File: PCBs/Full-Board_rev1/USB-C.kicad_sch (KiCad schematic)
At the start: 5 parts, among them J1 TYPE-C-31-M-12

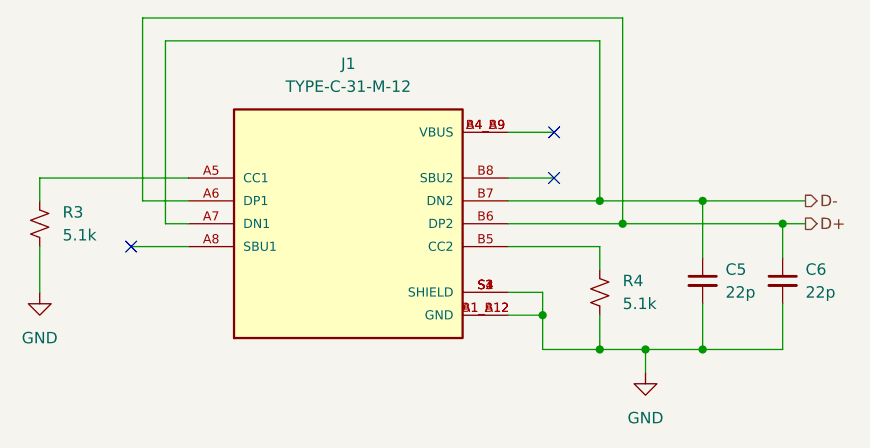
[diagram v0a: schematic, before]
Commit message: added ESP32 peripherals
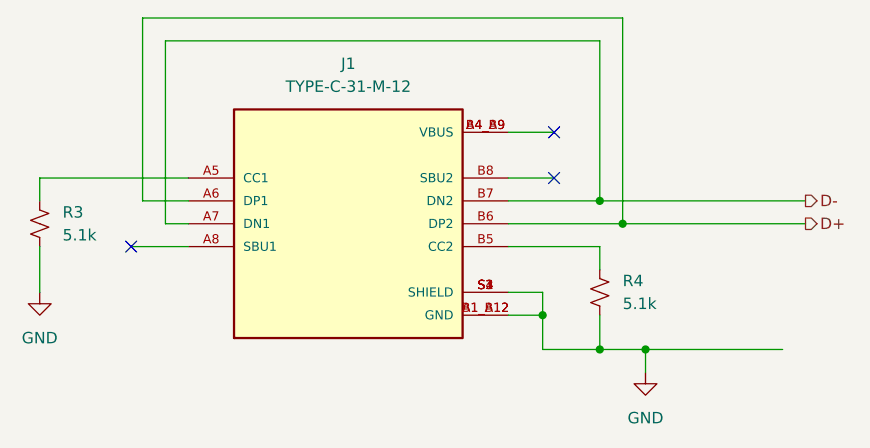
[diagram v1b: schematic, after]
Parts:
- removed C5, C6: 22p, symbol Device:C_Small
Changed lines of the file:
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@@
-	)
-	(junction
-		(at 180.34 115.57)
-		(diameter 0)
-		(color 0 0 0 0)
-	)
-	(junction
-		(at 189.23 101.6)
-		(diameter 0)
-		(color 0 0 0 0)
 	)
 	(junction
@@
 	)
 	(junction
-		(at 180.34 99.06)
-		(diameter 0)
-		(color 0 0 0 0)
-	)
-	(junction
 		(at 168.91 115.57)
 		(diameter 0)
@@
 	(wire
 		(pts
-			(xy 171.45 101.6) (xy 189.23 101.6)
+			(xy 171.45 101.6) (xy 191.77 101.6)
 		)
 		(stroke
@@
 	(wire
 		(pts
-			(xy 180.34 115.57) (xy 189.23 115.57)
-		)
-		(stroke
-			(width 0)
-			(type default)
-		)
-	)
-	(wire
-		(pts
 			(xy 158.75 96.52) (xy 163.83 96.52)
 		)
@@
 	(wire
 		(pts
-			(xy 180.34 99.06) (xy 191.77 99.06)
-		)
-		(stroke
-			(width 0)
-			(type default)
-		)
-	)
-	(wire
-		(pts
 			(xy 158.75 101.6) (xy 171.45 101.6)
 		)
@@
 	(wire
 		(pts
-			(xy 168.91 99.06) (xy 180.34 99.06)
+			(xy 168.91 99.06) (xy 191.77 99.06)
 		)
 		(stroke
@@
 	(wire
 		(pts
-			(xy 189.23 115.57) (xy 189.23 110.49)
-		)
-		(stroke
-			(width 0)
-			(type default)
-		)
-	)
-	(wire
-		(pts
 			(xy 158.75 99.06) (xy 168.91 99.06)
 		)
@@
 	(wire
 		(pts
-			(xy 173.99 115.57) (xy 180.34 115.57)
+			(xy 173.99 115.57) (xy 189.23 115.57)
 		)
 		(stroke
@@
 	(wire
 		(pts
-			(xy 189.23 101.6) (xy 189.23 105.41)
-		)
-		(stroke
-			(width 0)
-			(type default)
-		)
-	)
-	(wire
-		(pts
 			(xy 116.84 104.14) (xy 123.19 104.14)
 		)
@@
 	(wire
 		(pts
-			(xy 189.23 101.6) (xy 191.77 101.6)
-		)
-		(stroke
-			(width 0)
-			(type default)
-		)
-	)
-	(wire
-		(pts
 			(xy 120.65 81.28) (xy 168.91 81.28)
 		)
@@
 		(pts
 			(xy 168.91 115.57) (xy 173.99 115.57)
-		)
-		(stroke
-			(width 0)
-			(type default)
-		)
-	)
-	(wire
-		(pts
-			(xy 180.34 110.49) (xy 180.34 115.57)
-		)
-		(stroke
-			(width 0)
-			(type default)
-		)
-	)
-	(wire
-		(pts
-			(xy 180.34 99.06) (xy 180.34 105.41)
 		)
 		(stroke
@@
 			)
 			(justify left)
-		)
-	)
-	(symbol
-		(lib_id "Device:C_Small")
-		(at 180.34 107.95 0)
-		(unit 1)
-		(exclude_from_sim no)
-		(in_bom yes)
-		(on_board yes)
-		(dnp no)
-		(fields_autoplaced yes)
-		(property "Reference" "C5"
-			(at 182.88 106.6862 0)
-			(effects
-				(font
-					(size 1.27 1.27)
-				)
-				(justify left)
-			)
-		)
-		(property "Value" "22p"
-			(at 182.88 109.2262 0)
-			(effects
-				(font
-					(size 1.27 1.27)
-				)
-				(justify left)
-			)
-		)
-		(property "Footprint" ""
-			(at 180.34 107.95 0)
-			(effects
-				(font
-					(size 1.27 1.27)
-				)
-				(hide yes)
-			)
-		)
-		(property "Datasheet" "~"
-			(at 180.34 107.95 0)
-			(effects
-				(font
-					(size 1.27 1.27)
-				)
-				(hide yes)
-			)
-		)
-		(property "Description" "Unpolarized capacitor, small symbol"
-			(at 180.34 107.95 0)
-			(effects
-				(font
-					(size 1.27 1.27)
-				)
-				(hide yes)
-			)
-		)
-		(pin "2"
-		)
-		(pin "1"
-		)
-		(instances
-			(project ""
-				(path "/2dd686ed-aa28-474a-bf3c-628eebb4b373/4c56a540-4f9c-4723-9763-cba6b0ba4e1b"
-					(reference "C5")
-					(unit 1)
-				)
-			)
 		)
 	)
@@
 					(unit 1)
 				)
-			)
-		)
-	)
-	(symbol
-		(lib_id "Device:C_Small")
-		(at 189.23 107.95 0)
-		(unit 1)
-		(exclude_from_sim no)
-		(in_bom yes)
-		(on_board yes)
-		(dnp no)
-		(fields_autoplaced yes)
-		(property "Reference" "C6"
-			(at 191.77 106.6862 0)
-			(effects
-				(font
-					(size 1.27 1.27)
-				)
-				(justify left)
-			)
-		)
-		(property "Value" "22p"
-			(at 191.77 109.2262 0)
-			(effects
-				(font
-					(size 1.27 1.27)
-				)
-				(justify left)
-			)
-		)
-		(property "Footprint" ""
-			(at 189.23 107.95 0)
-			(effects
-				(font
-					(size 1.27 1.27)
-				)
-				(hide yes)
-			)
-		)
-		(property "Datasheet" "~"
-			(at 189.23 107.95 0)
-			(effects
-				(font
-					(size 1.27 1.27)
-				)
-				(hide yes)
-			)
-		)
-		(property "Description" "Unpolarized capacitor, small symbol"
-			(at 189.23 107.95 0)
-			(effects
-				(font
-					(size 1.27 1.27)
-				)
-				(hide yes)
-			)
-		)
-		(pin "1"
-		)
-		(pin "2"
-		)
-		(instances
-			(project ""
-				(path "/2dd686ed-aa28-474a-bf3c-628eebb4b373/4c56a540-4f9c-4723-9763-cba6b0ba4e1b"
-					(reference "C6")
-					(unit 1)
-				)

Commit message: Added footprints for main board components
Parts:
- R3, R4: footprint (none) -> Connector_PinHeader_2.54mm:PinHeader_1x02_P2.54mm_Vertical
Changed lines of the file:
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@@
 			)
 		)
-		(property "Footprint" ""
+		(property "Footprint" "Connector_PinHeader_2.54mm:PinHeader_1x02_P2.54mm_Vertical"
 			(at 106.68 101.6 0)
 			(effects
@@
 			)
 		)
-		(property "Footprint" ""
+		(property "Footprint" "Connector_PinHeader_2.54mm:PinHeader_1x02_P2.54mm_Vertical"
 			(at 168.91 109.22 0)
 			(effects

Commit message: Redid some faulty footprint assignments
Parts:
- R3, R4: footprint Connector_PinHeader_2.54mm:PinHeader_1x02_P2.54mm_Vertical -> Resistor_THT:R_Axial_DIN0207_L6.3mm_D2.5mm_P2.54mm_Vertical
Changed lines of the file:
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@@
 			)
 		)
-		(property "Footprint" "Connector_PinHeader_2.54mm:PinHeader_1x02_P2.54mm_Vertical"
+		(property "Footprint" "Resistor_THT:R_Axial_DIN0207_L6.3mm_D2.5mm_P2.54mm_Vertical"
 			(at 106.68 101.6 0)
 			(effects
@@
 			)
 		)
-		(property "Footprint" "Connector_PinHeader_2.54mm:PinHeader_1x02_P2.54mm_Vertical"
+		(property "Footprint" "Resistor_THT:R_Axial_DIN0207_L6.3mm_D2.5mm_P2.54mm_Vertical"
 			(at 168.91 109.22 0)
 			(effects

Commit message: restructured main layout, needs some cleanup still
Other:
- title: (none) -> SwarmSolve PCB
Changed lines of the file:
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@@
 	(generator_version "9.0")
 	(paper "A4")
+	(title_block
+		(title "SwarmSolve PCB")
+		(date "2025-08-26")
+		(rev "1")
+	)
 	(junction
 		(at 168.91 99.06)

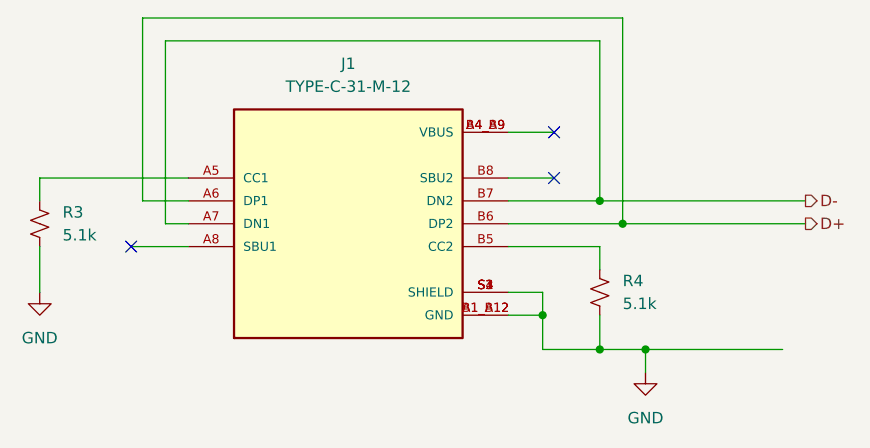
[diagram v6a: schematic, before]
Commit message: cleaned up schematic, everything is directly connected that can be, otherwise ports are used
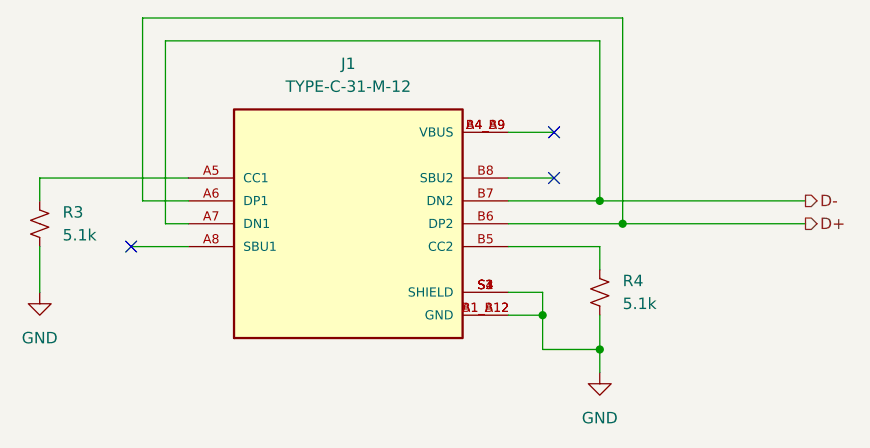
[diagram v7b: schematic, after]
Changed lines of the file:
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@@
-	)
-	(junction
-		(at 173.99 115.57)
-		(diameter 0)
-		(color 0 0 0 0)
 	)
 	(junction
@@
 	(wire
 		(pts
-			(xy 173.99 115.57) (xy 189.23 115.57)
-		)
-		(stroke
-			(width 0)
-			(type default)
-		)
-	)
-	(wire
-		(pts
 			(xy 118.11 99.06) (xy 118.11 78.74)
 		)
@@
 	(wire
 		(pts
-			(xy 173.99 118.11) (xy 173.99 115.57)
+			(xy 168.91 118.11) (xy 168.91 115.57)
 		)
 		(stroke
@@
 		(pts
 			(xy 162.56 115.57) (xy 168.91 115.57)
-		)
-		(stroke
-			(width 0)
-			(type default)
-		)
-	)
-	(wire
-		(pts
-			(xy 168.91 115.57) (xy 173.99 115.57)
 		)
 		(stroke
@@
 	(symbol
 		(lib_id "power:GND")
-		(at 173.99 118.11 0)
+		(at 168.91 118.11 0)
 		(unit 1)
 		(exclude_from_sim no)
@@
 		(fields_autoplaced yes)
 		(property "Reference" "#PWR08"
-			(at 173.99 124.46 0)
+			(at 168.91 124.46 0)
 			(effects
 				(font
@@
 		)
 		(property "Value" "GND"
-			(at 173.99 123.19 0)
+			(at 168.91 123.19 0)
 			(effects
 				(font
@@
 		)
 		(property "Footprint" ""
-			(at 173.99 118.11 0)
+			(at 168.91 118.11 0)
 			(effects
 				(font
@@
 		)
 		(property "Datasheet" ""
-			(at 173.99 118.11 0)
+			(at 168.91 118.11 0)
 			(effects
 				(font
@@
 		)
 		(property "Description" "Power symbol creates a global label with name \"GND\" , ground"
-			(at 173.99 118.11 0)
-			(effects
-				(font
+			(at 168.91 118.11 0)
+			(effects
+				(font
